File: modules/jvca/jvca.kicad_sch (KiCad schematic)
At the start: 6 parts

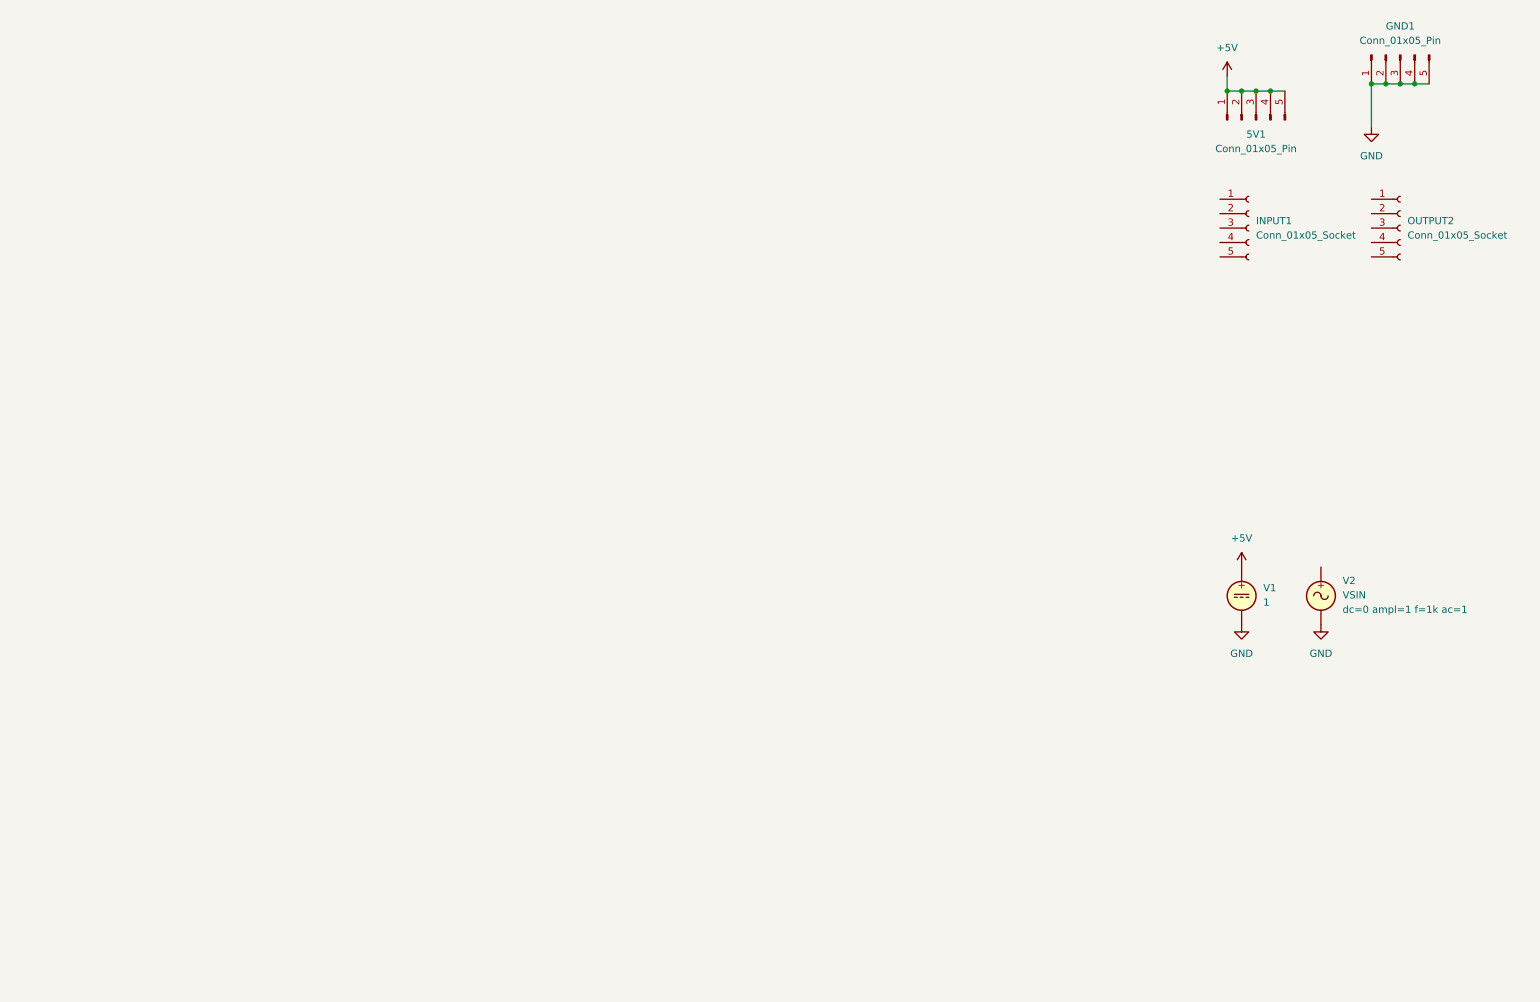
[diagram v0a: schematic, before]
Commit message: Implement the basic setup. CV support is not done and there are no CV control implemented.
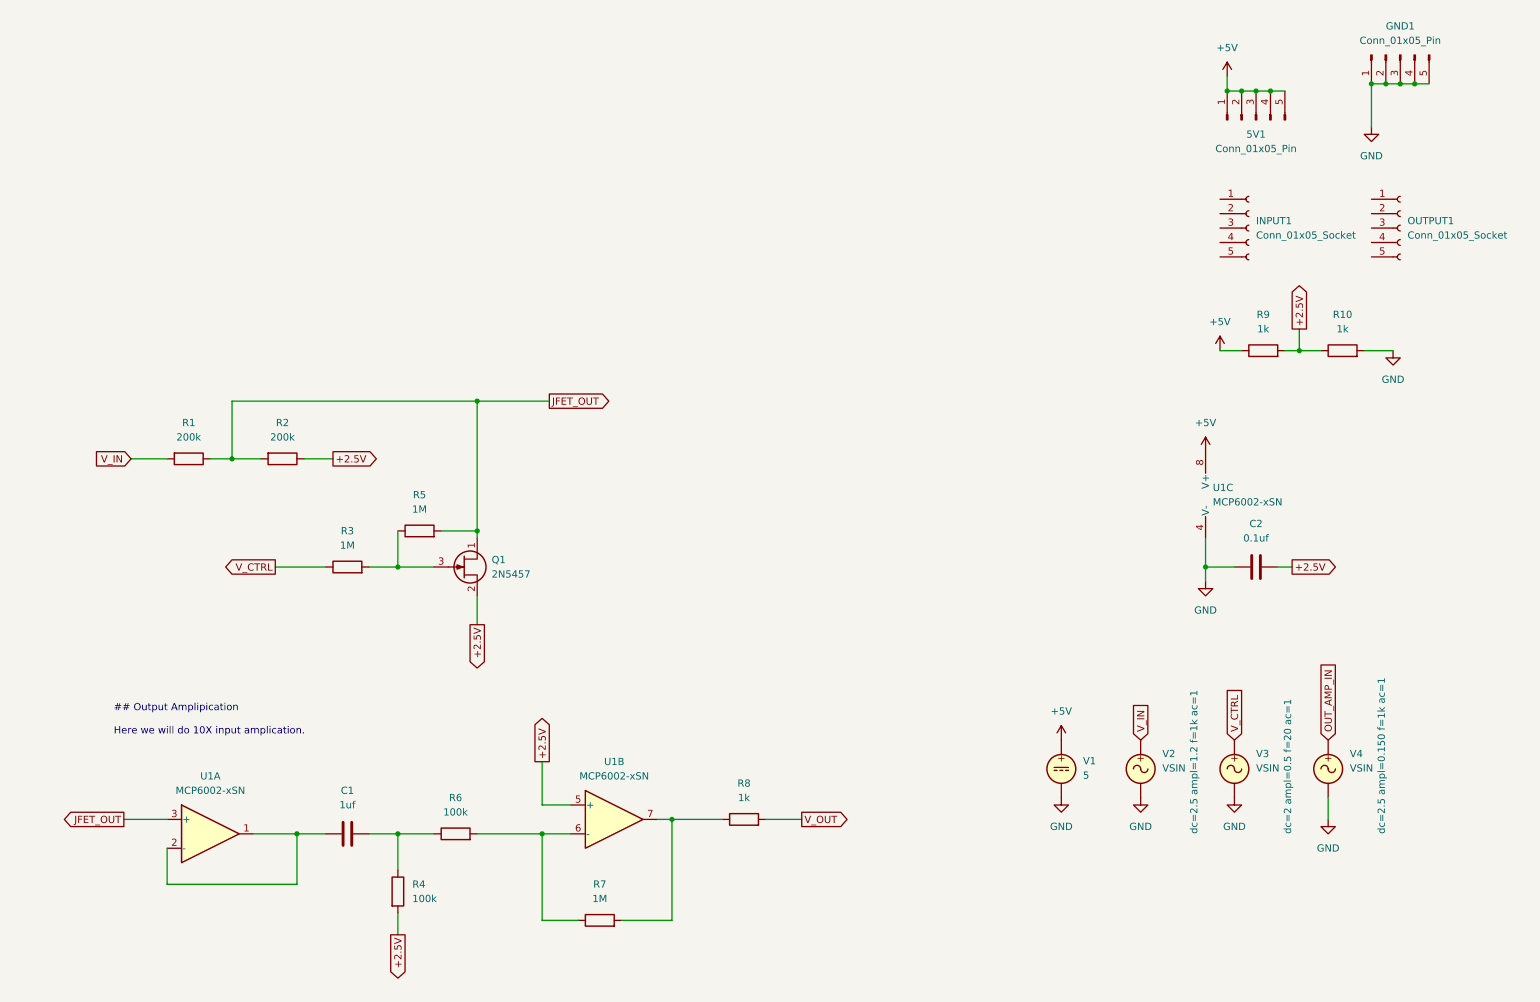
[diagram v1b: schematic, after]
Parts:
- added C1: 1uf, symbol Device:C
- added C2: 0.1uf, symbol Device:C
- added Q1: 2N5457, Package_TO_SOT_SMD:SOT-23, symbol Transistor_FET:BSR56
- added R1, R2: 200k, symbol Device:R
- added R10, R8, R9: 1k, symbol Device:R
- added R3, R5, R7: 1M, symbol Device:R
- added R4, R6: 100k, symbol Device:R
- added U1: MCP6002-xSN, symbol Amplifier_Operational:MCP6002-xSN
- added V3, V4: VSIN, symbol Simulation_SPICE:VSIN
- V1: value 1 -> 5
- renumbered OUTPUT2 to OUTPUT1
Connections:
- net +5V: now also R9.1, U1.8 (V+)
- net GND: now also C2.1, R10.2, U1.4 (V-), V3.2, V4.2
- net V_IN: now reaches V2.1
- net V_IN: now also R1.2
- new net: Q1.3 (G), R3.2, R5.1
- new net: C1.1, U1.1, U1.2 (-)
- new net: C1.2, R4.1, R6.1
- new net: R6.2, R7.1, U1.6 (-)
- new net: R7.2, R8.1, U1.7
- new net +2.5V: C2.2, Q1.2 (S), R10.1, R2.1, R4.2, R9.2, U1.5 (+)
- new net JFET_OUT: Q1.1 (D), R1.1, R2.2, R5.2, U1.3 (+)
- new net OUT_AMP_IN: V4.1
- new net V_CTRL: R3.1, V3.1
- new net V_OUT: R8.2
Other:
- note added: "## Output Amplipication Here we will do 10X input amplication."
- moved on the sheet: V1, V2

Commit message: Finish the jvca signal handling.
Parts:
- added C3: 0.1uf, symbol Device:C
- added R2: 22k, symbol Device:R
- added U2: MCP6002-xSN, symbol Amplifier_Operational:MCP6002-xSN
- C1: value 1uf -> 0.1uf
- R3: renamed from R2; value 200k -> 100k
- R5: renamed from R6; value 100k -> 22k
- R8: renamed from R7; value 1M -> 200k
- renumbered R9 to R10, R10 to R11, R3 to R6, R5 to R7, R8 to R9
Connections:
- net +2.5V: now also C3.2, U2.3 (+); no longer R3.1
- net +5V: now also U2.8 (V+)
- net GND: now also C3.1, U2.4 (V-)
- net JFET_OUT: now also R3.1; no longer R1.1, R3.2
- new net: R2.1, R3.2, U2.1
- new net: R1.1, R2.2, U2.2 (-)
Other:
- note added: "## Input Attenuation Here we will do 8X input attenuation. This way, we can reduce the distrotion introduce by JFET. Idea is to keep the JFET amplitude ~200mv"
- note added: "## Output Amplipication Here we will do 8X input amplication."
- note removed: "## Output Amplipication Here we will do 10X input amplication."
- moved on the sheet: Q1, R3, R6, R7, U1A

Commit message: Add CV controlling support
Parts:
- added C4: 4.7uf, symbol Device:C
- added R12, R13: 51k, symbol Device:R
- added R14: 2k, symbol Device:R
- added R15: 1k, symbol Device:R
- added R16: 100k, symbol Device:R
- added RV1: 1M, symbol Device:R_Potentiometer
- added RV2: 1k, symbol Device:R_Potentiometer
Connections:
- net +2.5V: now also U2.5 (+)
- net +5V: now also R14.2
- net GND: now also R15.1
- net at U2.6 (-): now also R12.2, R13.1
- net JFET_CV: now reaches U2.7
- net JFET_CV: now also R6.1, C4.1, C4.2, R12.1, R16.2
- net V_CTRL renamed CV
- net CV: now also RV1.3; no longer R6.1
- new net: R13.2, RV1.2
- new net: R15.2, RV2.1
- new net: R16.1, RV2.2
- new net: R14.1, RV2.3
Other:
- note added: "## CV Controlling Here we do CV gain(RV1) and bias control(RV2). We also invert the signal because JFET needs inverted signal."
- moved on the sheet: U2B

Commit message: Assigned footprints
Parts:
- C1: footprint (none) -> Capacitor_SMD:C_0402_1005Metric
- C2: renamed from C4; footprint (none) -> Capacitor_SMD:C_1206_3216Metric
- C3: renamed from C2; footprint (none) -> Capacitor_SMD:C_0402_1005Metric
- C4: renamed from C3; footprint (none) -> Capacitor_SMD:C_0402_1005Metric
- Q1: footprint Package_TO_SOT_SMD:SOT-23 -> Package_TO_SOT_THT:TO-92L_HandSolder
- R1, R2, R4: footprint (none) -> Resistor_SMD:R_0402_1005Metric
- R10: renamed from R16; footprint (none) -> Resistor_SMD:R_0402_1005Metric
- R11: renamed from R7; footprint (none) -> Resistor_SMD:R_0402_1005Metric
- R12: renamed from R8; footprint (none) -> Resistor_SMD:R_0402_1005Metric
- R13: renamed from R15; footprint (none) -> Resistor_SMD:R_0402_1005Metric
- R14: renamed from R9; footprint (none) -> Resistor_SMD:R_0402_1005Metric
- R15: renamed from R10; footprint (none) -> Resistor_SMD:R_0402_1005Metric
- R16: renamed from R11; footprint (none) -> Resistor_SMD:R_0402_1005Metric
- R3: renamed from R13; footprint (none) -> Resistor_SMD:R_0402_1005Metric
- R5: renamed from R12; footprint (none) -> Resistor_SMD:R_0402_1005Metric
- R6: renamed from R5; footprint (none) -> Resistor_SMD:R_0402_1005Metric
- R7: renamed from R3; footprint (none) -> Resistor_SMD:R_0402_1005Metric
- R8: renamed from R14; footprint (none) -> Resistor_SMD:R_0402_1005Metric
- R9: renamed from R6; footprint (none) -> Resistor_SMD:R_0402_1005Metric
- RV1, RV2: footprint (none) -> BreadModular_Pots:Potentiometer_RV09
- U1, U2: footprint (none) -> Package_SO:SOIC-8-1EP_3.9x4.9mm_P1.27mm_EP2.29x3mm
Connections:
- net CV: now also INPUT1.2 (Pin_2)
- net JFET_CV: no longer C2.1, R5.1, U2.7
- net V_IN: now also INPUT1.1 (Pin_1)
- net V_OUT: now also OUTPUT1.1 (Pin_1), OUTPUT1.2 (Pin_2), OUTPUT1.3 (Pin_3), OUTPUT1.4 (Pin_4), OUTPUT1.5 (Pin_5)
- net at INPUT1.3 (Pin_3): now also INPUT1.4 (Pin_4), INPUT1.5 (Pin_5)
- new net: C2.1, R5.1, U2.7
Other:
- moved on the sheet: OUTPUT1
